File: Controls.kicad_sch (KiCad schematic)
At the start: 10 parts, among them J1 FOOTSWITCH, J2 PCIE_FX, SW1 SW_SPDT, SW2 SW_SPDT, SW3 SW_SPDT, X1 PEDAL_COMBO_TOP

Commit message: Initial layout
Finished the initial PCB layout.
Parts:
- removed SW3: SW_SPDT, Custom_Parts:SW_SPDT, symbol Switch:SW_SPDT
- removed X1: PEDAL_COMBO_TOP, Custom_Parts:PEDAL_COMBO_TOP, symbol Custom_Parts:PEDAL_COMBO_TOP
- added D4, D5: H15VSD3B, Diode_SMD:D_SOD-323, symbol Device:D_TVS
- added J1: JACK CONNECTOR, Custom_Parts:HEADER_THROUGH_2x03_P2.54mm, symbol Connector_Generic:Conn_02x03_Counter_Clockwise
- added SW3, SW4: MINI_SW, Custom_Parts:MINI_TOGGLE_SHIELD, symbol Custom_Parts:SW_SPDT_MountingPin
- RV4: value RS4511 -> RK09L; footprint Custom_Parts:RS45111A900F -> Custom_Parts:POT_SINGLE_VERTICAL_6X15
- renumbered J1 to J2, J2 to J3
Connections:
- net SW3_NC is gone; now on net GND: J3.50 (GND)
- net +VCC_FILT: now also J2.5 (Pin_5), J3.10 (VCC), J3.12 (VCC); no longer J2.2 (Pin_2), J2.8 (Pin_8), J3.11 (VCC), J3.9 (VCC)
- net -VSS: now also J3.2 (VSS), J3.4 (VSS); no longer J3.1 (VSS), J3.3 (VSS)
- net AUDIO_IN: now also J2.6 (Pin_6), D5.1 (A1), J1.1 (Pin_1); no longer J2.1 (Pin_1)
- net AUDIO_OUT: now also J2.1 (Pin_1), D4.1 (A1), J1.3 (Pin_3); no longer J2.6 (Pin_6)
- net FX_IN: now also J2.4 (Pin_4), J3.18 (B1); no longer J2.3 (Pin_3), J3.28 (B4)
- net FX_OUT: now also J2.3 (Pin_3), J3.52 (B12); no longer J2.4 (Pin_4), J3.32 (B5)
- net GND: now also J2.2 (Pin_2), J3.1 (GND), J3.11 (GND), J3.14 (GND), J3.16 (GND), J3.19 (GND), J3.20 (GND), J3.25 (GND), J3.26 (GND), J3.3 (GND), J3.31 (GND), J3.32 (GND), J3.37 (GND), J3.38 (GND), J3.43 (GND), J3.44 (GND), J3.49 (GND), J3.6 (GND), J3.8 (GND), J3.9 (GND), D4.2 (A2), D5.2 (A2), J1.2 (Pin_2); no longer J2.5 (Pin_5), J3.10 (GND), J3.12 (GND), J3.13 (GND), J3.15 (GND), J3.17 (GND), J3.18 (GND), J3.2 (GND), J3.23 (GND), J3.24 (GND), J3.29 (GND), J3.30 (GND), J3.35 (GND), J3.36 (GND), J3.4 (GND), J3.41 (GND), J3.42 (GND), J3.47 (GND), J3.48 (GND), J3.5 (GND), J3.7 (GND)
- net P1_H: now also J3.17 (A1); no longer J3.19 (A1)
- net P1_L: now also J3.23 (A3); no longer J3.25 (A3)
- net P2_H: now also J3.35 (A7); no longer J3.37 (A7)
- net P2_L: now also J3.41 (A9); no longer J3.43 (A9)
- net P3_H: now also J3.22 (B2); no longer J3.20 (B1)
- net P3_L: now also J3.28 (B4); no longer J3.26 (B3)
- net P3_W: now also J3.24 (B3); no longer J3.22 (B2)
- net P4_H: now also J3.42 (B9); no longer J3.38 (B7)
- net P4_L: now also J3.48 (B11); no longer J3.44 (B9)
- net P4_W: now also J3.46 (B10); no longer J3.40 (B8)
- net SW1_NC: now also J3.29 (A5); no longer J3.31 (A5)
- net SW2_NC: now also J3.47 (A11); no longer J3.49 (A11)
- net SW3_IN: now also J3.30 (B5), SW3.2 (B); no longer J3.46 (B10)
- net SW3_NO: now also J3.34 (B6), SW3.3 (C); no longer J3.52 (B12)
- new net +VDC: J1.5 (Pin_5)
- new net SW4_IN: J3.36 (B7), SW4.2 (B)
- new net SW4_NO: J3.40 (B8), SW4.3 (C)
- no-connect marks 18 -> 20
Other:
- moved on the sheet: J2, J3

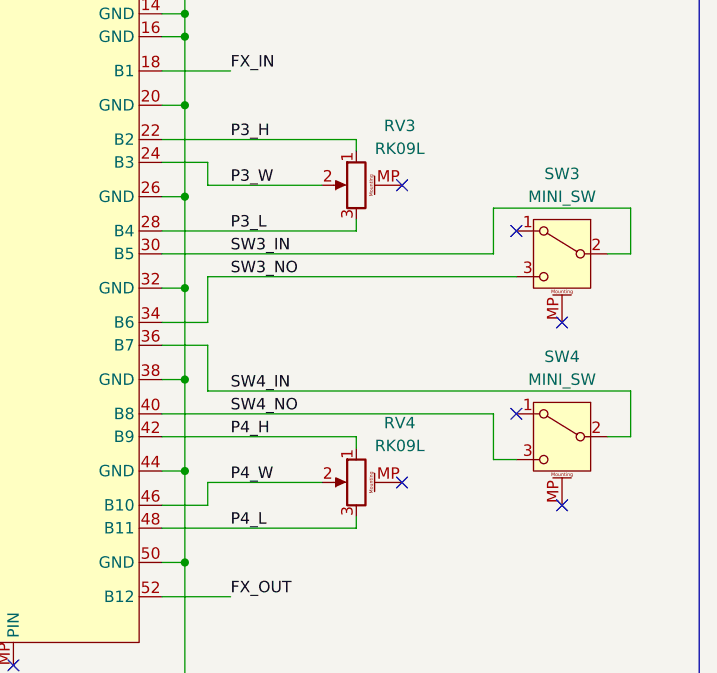
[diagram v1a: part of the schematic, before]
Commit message: Filtering section and layout
Updated the PCB layout.
Added additional input voltage filtering.
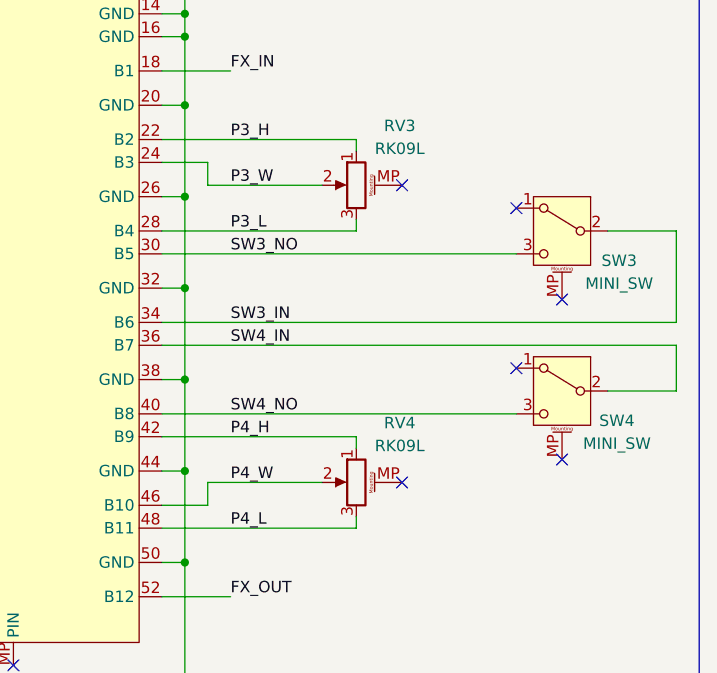
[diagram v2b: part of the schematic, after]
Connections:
- net SW3_IN: now also J3.34 (B6); no longer J3.30 (B5)
- net SW3_NO: now also J3.30 (B5); no longer J3.34 (B6)
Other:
- moved on the sheet: SW3, SW4
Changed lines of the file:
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@@
 	)
 	(no_connect
-		(at 224.79 106.68)
+		(at 224.79 101.6)
 	)
 	(no_connect
@@
 	)
 	(no_connect
-		(at 229.87 96.52)
+		(at 229.87 93.98)
 	)
 	(no_connect
@@
 	)
 	(no_connect
-		(at 229.87 116.84)
+		(at 229.87 111.76)
 	)
 	(no_connect
@@
 	)
 	(no_connect
-		(at 224.79 86.36)
-	)
-	(wire
-		(pts
-			(xy 185.42 88.9) (xy 222.25 88.9)
-		)
-		(stroke
-			(width 0)
-			(type default)
-		)
+		(at 224.79 83.82)
 	)
 	(wire
@@
 	(wire
 		(pts
+			(xy 234.95 86.36) (xy 242.57 86.36)
+		)
+		(stroke
+			(width 0)
+			(type default)
+		)
+	)
+	(wire
+		(pts
 			(xy 125.73 91.44) (xy 123.19 91.44)
 		)
@@
 	(wire
 		(pts
-			(xy 237.49 83.82) (xy 222.25 83.82)
-		)
-		(stroke
-			(width 0)
-			(type default)
-		)
-	)
-	(wire
-		(pts
 			(xy 80.01 120.65) (xy 82.55 120.65)
 		)
@@
 	(wire
 		(pts
-			(xy 190.5 104.14) (xy 190.5 99.06)
-		)
-		(stroke
-			(width 0)
-			(type default)
-		)
-	)
-	(wire
-		(pts
 			(xy 135.89 88.9) (xy 152.4 88.9)
 		)
@@
 	(wire
 		(pts
-			(xy 224.79 91.44) (xy 190.5 91.44)
-		)
-		(stroke
-			(width 0)
-			(type default)
-		)
-	)
-	(wire
-		(pts
 			(xy 185.42 62.23) (xy 187.96 62.23)
 		)
@@
 	(wire
 		(pts
-			(xy 237.49 88.9) (xy 237.49 83.82)
-		)
-		(stroke
-			(width 0)
-			(type default)
-		)
-	)
-	(wire
-		(pts
 			(xy 185.42 82.55) (xy 187.96 82.55)
 		)
@@
 	(wire
 		(pts
-			(xy 190.5 104.14) (xy 237.49 104.14)
-		)
-		(stroke
-			(width 0)
-			(type default)
-		)
-	)
-	(wire
-		(pts
 			(xy 81.28 52.07) (xy 57.15 52.07)
 		)
@@
 	(wire
 		(pts
+			(xy 185.42 88.9) (xy 224.79 88.9)
+		)
+		(stroke
+			(width 0)
+			(type default)
+		)
+	)
+	(wire
+		(pts
 			(xy 187.96 64.77) (xy 187.96 72.39)
 		)
@@
 	(wire
 		(pts
-			(xy 222.25 83.82) (xy 222.25 88.9)
-		)
-		(stroke
-			(width 0)
-			(type default)
-		)
-	)
-	(wire
-		(pts
 			(xy 185.42 52.07) (xy 187.96 52.07)
 		)
@@
 	(wire
 		(pts
-			(xy 190.5 91.44) (xy 190.5 96.52)
-		)
-		(stroke
-			(width 0)
-			(type default)
-		)
-	)
-	(wire
-		(pts
 			(xy 134.62 73.66) (xy 147.32 73.66)
 		)
@@
 	(wire
 		(pts
+			(xy 185.42 96.52) (xy 242.57 96.52)
+		)
+		(stroke
+			(width 0)
+			(type default)
+		)
+	)
+	(wire
+		(pts
 			(xy 130.81 99.06) (xy 152.4 99.06)
 		)
@@
 	(wire
 		(pts
+			(xy 185.42 106.68) (xy 224.79 106.68)
+		)
+		(stroke
+			(width 0)
+			(type default)
+		)
+	)
+	(wire
+		(pts
 			(xy 67.31 125.73) (xy 82.55 125.73)
 		)
@@
 	(wire
 		(pts
-			(xy 222.25 111.76) (xy 222.25 106.68)
-		)
-		(stroke
-			(width 0)
-			(type default)
-		)
-	)
-	(wire
-		(pts
 			(xy 190.5 81.28) (xy 190.5 78.74)
 		)
@@
 	(wire
 		(pts
-			(xy 224.79 111.76) (xy 222.25 111.76)
-		)
-		(stroke
-			(width 0)
-			(type default)
-		)
-	)
-	(wire
-		(pts
 			(xy 187.96 49.53) (xy 187.96 52.07)
 		)
@@
 	(wire
 		(pts
+			(xy 242.57 86.36) (xy 242.57 96.52)
+		)
+		(stroke
+			(width 0)
+			(type default)
+		)
+	)
+	(wire
+		(pts
 			(xy 185.42 123.19) (xy 187.96 123.19)
 		)
@@
 	(wire
 		(pts
-			(xy 190.5 99.06) (xy 185.42 99.06)
+			(xy 185.42 99.06) (xy 242.57 99.06)
 		)
 		(stroke
@@
 	(wire
 		(pts
-			(xy 237.49 109.22) (xy 237.49 104.14)
+			(xy 242.57 104.14) (xy 242.57 99.06)
 		)
 		(stroke
@@
 	(wire
 		(pts
-			(xy 234.95 88.9) (xy 237.49 88.9)
-		)
-		(stroke
-			(width 0)
-			(type default)
-		)
-	)
-	(wire
-		(pts
 			(xy 149.86 55.88) (xy 152.4 55.88)
 		)
@@
 	(wire
 		(pts
-			(xy 190.5 96.52) (xy 185.42 96.52)
-		)
-		(stroke
-			(width 0)
-			(type default)
-		)
-	)
-	(wire
-		(pts
 			(xy 147.32 124.46) (xy 147.32 127)
 		)
@@
 	(wire
 		(pts
-			(xy 185.42 106.68) (xy 222.25 106.68)
-		)
-		(stroke
-			(width 0)
-			(type default)
-		)
-	)
-	(wire
-		(pts
 			(xy 207.01 85.09) (xy 207.01 86.36)
 		)
@@
 	(wire
 		(pts
-			(xy 234.95 109.22) (xy 237.49 109.22)
+			(xy 234.95 104.14) (xy 242.57 104.14)
 		)
 		(stroke
@@
 		)
 	)
+	(label "SW3_IN"
+		(at 193.04 96.52 0)
+		(effects
+			(font
+				(size 1.27 1.27)
+			)
+			(justify left bottom)
+		)
+	)
 	(label "AUDIO_OUT"
 		(at 80.01 115.57 180)
@@
 	)
 	(label "SW3_NO"
-		(at 193.04 91.44 0)
+		(at 193.04 88.9 0)
 		(effects
 			(font
@@
 		)
 	)
-	(label "SW3_IN"
-		(at 193.04 88.9 0)
-		(effects
-			(font
-				(size 1.27 1.27)
-			)
-			(justify left bottom)
-		)
-	)
 	(label "P3_H"
 		(at 193.04 76.2 0)
@@
 	)
 	(label "SW4_IN"
-		(at 193.04 104.14 0)
+		(at 193.04 99.06 0)
 		(effects
 			(font
@@
 	(symbol
 		(lib_id "Custom_Parts:SW_SPDT_MountingPin")
-		(at 229.87 88.9 0)
+		(at 229.87 86.36 0)
 		(mirror y)
 		(unit 1)
@@
 		(dnp no)
 		(property "Reference" "SW3"
-			(at 229.87 80.01 0)
+			(at 236.22 89.662 0)
 			(show_name no)
 			(do_not_autoplace no)
@@
 		)
 		(property "Value" "MINI_SW"
-			(at 229.87 82.55 0)
+			(at 236.22 92.202 0)
 			(show_name no)
 			(do_not_autoplace no)
@@
 		)
 		(property "Footprint" "Custom_Parts:MINI_TOGGLE_SHIELD"
-			(at 229.87 88.9 0)
+			(at 229.87 86.36 0)
 			(hide yes)
 			(show_name no)
@@
 		)
 		(property "Datasheet" ""
-			(at 229.87 96.52 0)
+			(at 229.87 93.98 0)
 			(hide yes)
 			(show_name no)
@@
 		)
 		(property "Description" "Switch, single pole double throw"
-			(at 229.87 88.9 0)
+			(at 229.87 86.36 0)
 			(hide yes)
 			(show_name no)
@@
 	(symbol
 		(lib_id "Custom_Parts:SW_SPDT_MountingPin")
-		(at 229.87 109.22 0)
+		(at 229.87 104.14 0)
 		(mirror y)
 		(unit 1)
@@
 		(dnp no)
 		(property "Reference" "SW4"
-			(at 229.87 100.33 0)
+			(at 235.966 107.442 0)
 			(show_name no)
 			(do_not_autoplace no)
@@
 		)
 		(property "Value" "MINI_SW"
-			(at 229.87 102.87 0)
+			(at 235.966 109.982 0)
 			(show_name no)
 			(do_not_autoplace no)
@@
 		)
 		(property "Footprint" "Custom_Parts:MINI_TOGGLE_SHIELD"
-			(at 229.87 109.22 0)
+			(at 229.87 104.14 0)
 			(hide yes)
 			(show_name no)
@@
 		)
 		(property "Datasheet" ""
-			(at 229.87 116.84 0)
+			(at 229.87 111.76 0)
 			(hide yes)
 			(show_name no)
@@
 		)
 		(property "Description" "Switch, single pole double throw"
-			(at 229.87 109.22 0)
+			(at 229.87 104.14 0)
 			(hide yes)
 			(show_name no)

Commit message: Board layout
Updated the layout of the power lines.
Updated the layout of the control signals.
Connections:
- net +VCC_FILT: now also J3.2 (VSS), J3.4 (VSS); no longer J3.10 (VCC), J3.12 (VCC)
- net -VSS: now also J3.10 (VCC), J3.12 (VCC); no longer J3.2 (VSS), J3.4 (VSS)
- net SW1_NC: now also J3.33 (A6); no longer J3.29 (A5)
- net SW1_NO: now also J3.29 (A5); no longer J3.33 (A6)
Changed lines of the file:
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@@
+	)
+	(junction
+		(at 187.96 43.18)
+		(diameter 0)
+		(color 0 0 0 0)
 	)
 	(junction
@@
 	)
 	(junction
-		(at 187.96 43.18)
-		(diameter 0)
-		(color 0 0 0 0)
-	)
-	(junction
 		(at 73.66 54.61)
 		(diameter 0)
@@
 	(wire
 		(pts
-			(xy 193.04 35.56) (xy 193.04 55.88)
+			(xy 193.04 40.64) (xy 193.04 55.88)
 		)
 		(stroke
@@
 	(wire
 		(pts
-			(xy 187.96 40.64) (xy 187.96 43.18)
+			(xy 187.96 35.56) (xy 187.96 43.18)
 		)
 		(stroke
@@
 		)
 	)
-	(label "SW1_NO"
+	(label "SW1_NC"
 		(at 137.16 93.98 0)
 		(effects
@@
 		)
 	)
-	(label "SW1_NC"
+	(label "SW1_NO"
 		(at 137.16 88.9 0)
 		(effects
@@
 	(symbol
 		(lib_id "power:VSS")
-		(at 187.96 40.64 0)
+		(at 193.04 40.64 0)
 		(unit 1)
 		(body_style 1)
@@
 		(fields_autoplaced yes)
 		(property "Reference" "#PWR021"
-			(at 187.96 44.45 0)
+			(at 193.04 44.45 0)
 			(hide yes)
 			(show_name no)
@@
 		)
 		(property "Value" "-VSS"
-			(at 187.96 35.56 0)
+			(at 193.04 35.56 0)
 			(show_name no)
 			(do_not_autoplace no)
@@
 		)
 		(property "Footprint" ""
-			(at 187.96 40.64 0)
+			(at 193.04 40.64 0)
 			(hide yes)
 			(show_name no)
@@
 		)
 		(property "Datasheet" ""
-			(at 187.96 40.64 0)
+			(at 193.04 40.64 0)
 			(hide yes)
 			(show_name no)
@@
 		)
 		(property "Description" "Power symbol creates a global label with name \"VSS\""
-			(at 187.96 40.64 0)
+			(at 193.04 40.64 0)
 			(hide yes)
 			(show_name no)
@@
 	(symbol
 		(lib_id "power:+3.3V")
-		(at 193.04 35.56 0)
+		(at 187.96 35.56 0)
 		(unit 1)
 		(body_style 1)
@@
 		(dnp no)
 		(property "Reference" "#PWR023"
-			(at 193.04 39.37 0)
+			(at 187.96 39.37 0)
 			(hide yes)
 			(show_name no)
@@
 		)
 		(property "Value" "+VCC_FILT"
-			(at 193.04 30.48 0)
+			(at 187.96 30.48 0)
 			(show_name no)
 			(do_not_autoplace no)
@@
 		)
 		(property "Footprint" ""
-			(at 193.04 35.56 0)
+			(at 187.96 35.56 0)
 			(hide yes)
 			(show_name no)
@@
 		)
 		(property "Datasheet" ""
-			(at 193.04 35.56 0)
+			(at 187.96 35.56 0)
 			(hide yes)
 			(show_name no)
@@
 		)
 		(property "Description" "Power symbol creates a global label with name \"+3.3V\""
-			(at 193.04 35.56 0)
+			(at 187.96 35.56 0)
 			(hide yes)
 			(show_name no)
@@
 		(lib_id "Switch:SW_SPDT")
 		(at 130.81 91.44 0)
+		(mirror x)
 		(unit 1)
 		(body_style 1)
@@
 		(in_pos_files yes)
 		(dnp no)
-		(fields_autoplaced yes)
 		(property "Reference" "SW1"
 			(at 130.81 82.55 0)
@@
 		)
 		(property "Datasheet" ""
-			(at 130.81 99.06 0)
-			(hide yes)
-			(show_name no)
+			(at 130.81 83.82 0)
+			(hide yes)
+			(show_name no)

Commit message: Layout and mounting
Connected all tracks in the layout.
Added a mounting standoff.
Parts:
- added H2: PCIE_MOUNT, Mounting_Wuerth:Mounting_Wuerth_WA-SMSI-M2_H1.5mm_9774015243, symbol Mechanical:MountingHole_Pad
- J3: footprint Custom_Parts:Mini PCI_Express -> Custom_Parts:Mini PCI_Express_Pads
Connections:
- no-connect marks 20 -> 21
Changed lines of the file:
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@@
 		)
 	)
+	(text_box "PCIE MOUNT"
+		(exclude_from_sim no)
+		(at 50.8 158.75 0)
+		(size 58.42 20.32)
+		(margins 0.9525 0.9525 0.9525 0.9525)
+		(stroke
+			(width 0)
+			(type solid)
+		)
+		(fill
+			(type none)
+		)
+		(effects
+			(font
+				(size 1.27 1.27)
+			)
+			(justify left top)
+		)
+	)
 	(text_box "EFFECT INTERFACE"
 		(exclude_from_sim no)
@@
 	)
 	(no_connect
+		(at 77.47 172.72)
+	)
+	(no_connect
 		(at 229.87 111.76)
 	)
@@
 	)
 	(symbol
+		(lib_id "Mechanical:MountingHole_Pad")
+		(at 77.47 170.18 0)
+		(unit 1)
+		(body_style 1)
+		(exclude_from_sim no)
+		(in_bom no)
+		(on_board yes)
+		(in_pos_files yes)
+		(dnp no)
+		(fields_autoplaced yes)
+		(property "Reference" "H2"
+			(at 80.01 167.6399 0)
+			(show_name no)
+			(do_not_autoplace no)
+			(effects
+				(font
+					(size 1.27 1.27)
+				)
+				(justify left)
+			)
+		)
+		(property "Value" "PCIE_MOUNT"
+			(at 80.01 170.1799 0)
+			(show_name no)
+			(do_not_autoplace no)
+			(effects
+				(font
+					(size 1.27 1.27)
+				)
+				(justify left)
+			)
+		)
+		(property "Footprint" "Mounting_Wuerth:Mounting_Wuerth_WA-SMSI-M2_H1.5mm_9774015243"
+			(at 77.47 170.18 0)
+			(hide yes)
+			(show_name no)
+			(do_not_autoplace no)
+			(effects
+				(font
+					(size 1.27 1.27)
+				)
+			)
+		)
+		(property "Datasheet" ""
+			(at 77.47 170.18 0)
+			(hide yes)
+			(show_name no)
+			(do_not_autoplace no)
+			(effects
+				(font
+					(size 1.27 1.27)
+				)
+			)
+		)
+		(property "Description" "Mounting Hole with connection"
+			(at 77.47 170.18 0)
+			(hide yes)
+			(show_name no)
+			(do_not_autoplace no)
+			(effects
+				(font
+					(size 1.27 1.27)
+				)
+			)
+		)
+		(pin "1"
+		)
+		(instances
+			(project "EffectsBase"
+				(path "/a2cd04b3-686a-4ef4-b876-d75449c48611/3b0bf6c7-4527-4110-8166-1b2049d6297e"
+					(reference "H2")
+					(unit 1)
+				)
+			)
+		)
+	)
+	(symbol
 		(lib_id "Custom_Parts:PCIeFX")
 		(at 168.91 85.09 0)
@@
 			)
 		)
-		(property "Footprint" "Custom_Parts:Mini PCI_Express"
+		(property "Footprint" "Custom_Parts:Mini PCI_Express_Pads"
 			(at 168.91 85.09 0)
 			(hide yes)

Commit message: Finished layout
Initial PCB layout iteration.
Updated the readme file.
Added board images.
Added output files.
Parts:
- removed J2: FOOTSWITCH, Custom_Parts:HEADER_THROUGH_2x06_P2.54mm, symbol Connector_Generic:Conn_02x06_Top_Bottom
- added H2, H3, H4: TOOL, MountingHole:ToolingHole_1.152mm, symbol Mechanical:MountingHole
- added J1: FOOTSWITCH, Custom_Parts:HEADER_THROUGH_2x05_P2.54mm, symbol Connector_Generic:Conn_02x05_Top_Bottom
- D4, D5: JLCPCB Part (none) -> C20615814; Manufacturer Part (none) -> H15VSD3B
- H1: renamed from H2; now not fitted
- J2: renamed from J1; JLCPCB Part (none) -> -; Manufacturer Part (none) -> -; now not fitted; now left out of the parts list
- J3: JLCPCB Part (none) -> C404126; Manufacturer Part (none) -> 91304-99-052R2
- RV1, RV2, RV3, RV4, SW1, SW2, SW3, SW4: JLCPCB Part (none) -> -; Manufacturer Part (none) -> -; now left out of the parts list
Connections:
- net +VCC_FILT: now also J1.3 (Pin_3)
- net AUDIO_IN: now also J1.5 (Pin_5)
- net AUDIO_OUT: now also J1.1 (Pin_1)
- net FX_IN: now also J1.4 (Pin_4)
- net FX_OUT: now also J1.2 (Pin_2)
- net GND: now also J1.8 (Pin_8)
- no-connect marks 21 -> 20
